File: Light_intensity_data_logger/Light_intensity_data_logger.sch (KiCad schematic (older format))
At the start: 23 parts, among them J1 Wire_to_Vbat, Q1 NTJD4001NT1G, Q2 NTJD4001NT1G, U1 BME280, U2 TCS34725FN, U3 TSL25911FN, U4 Teensy3.6

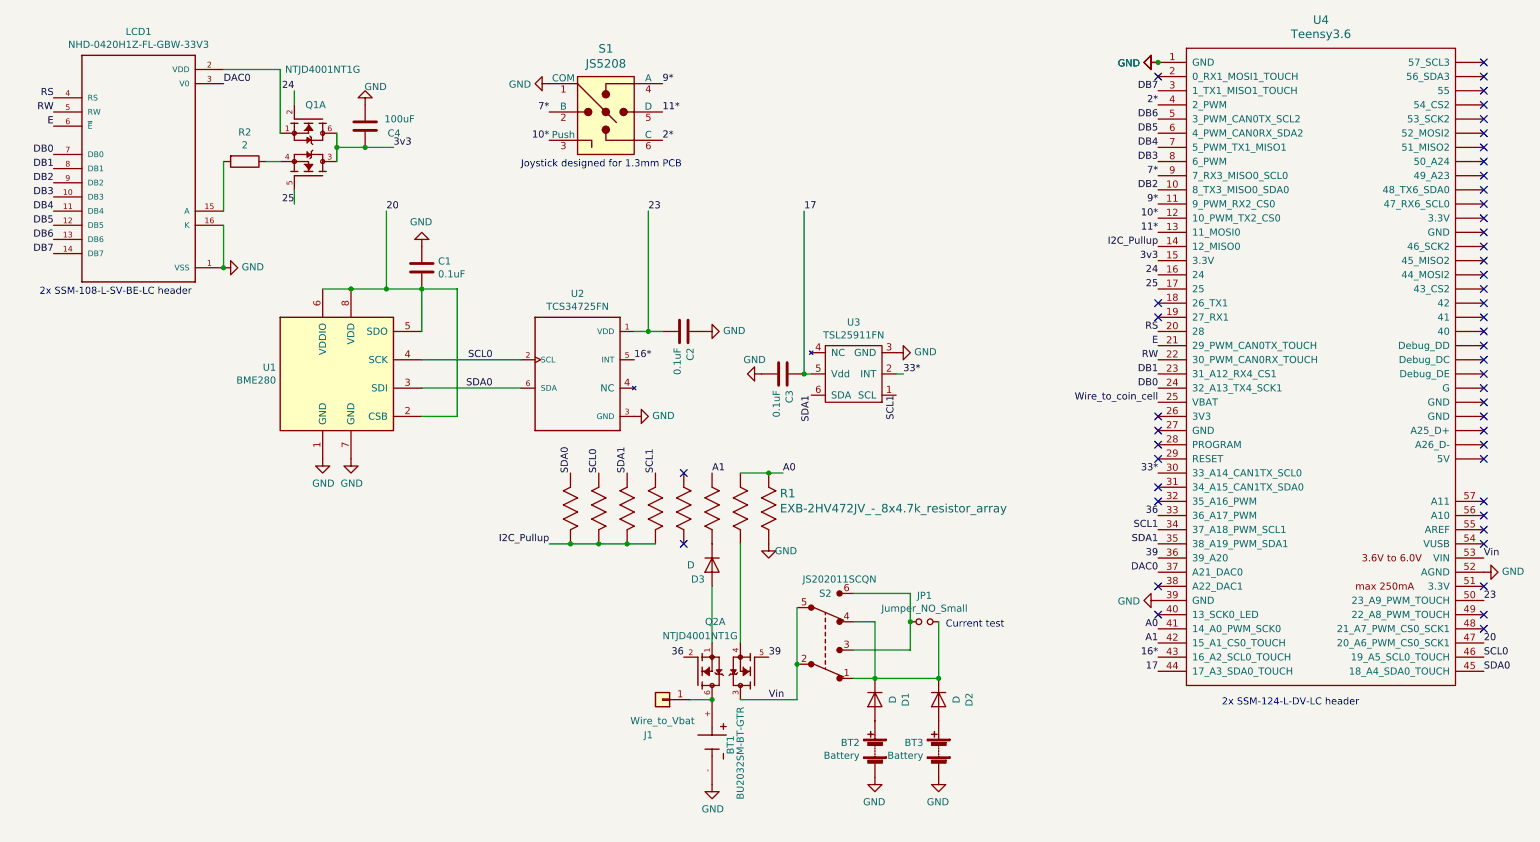
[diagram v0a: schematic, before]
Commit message: Rewire LED gate to PWM channel
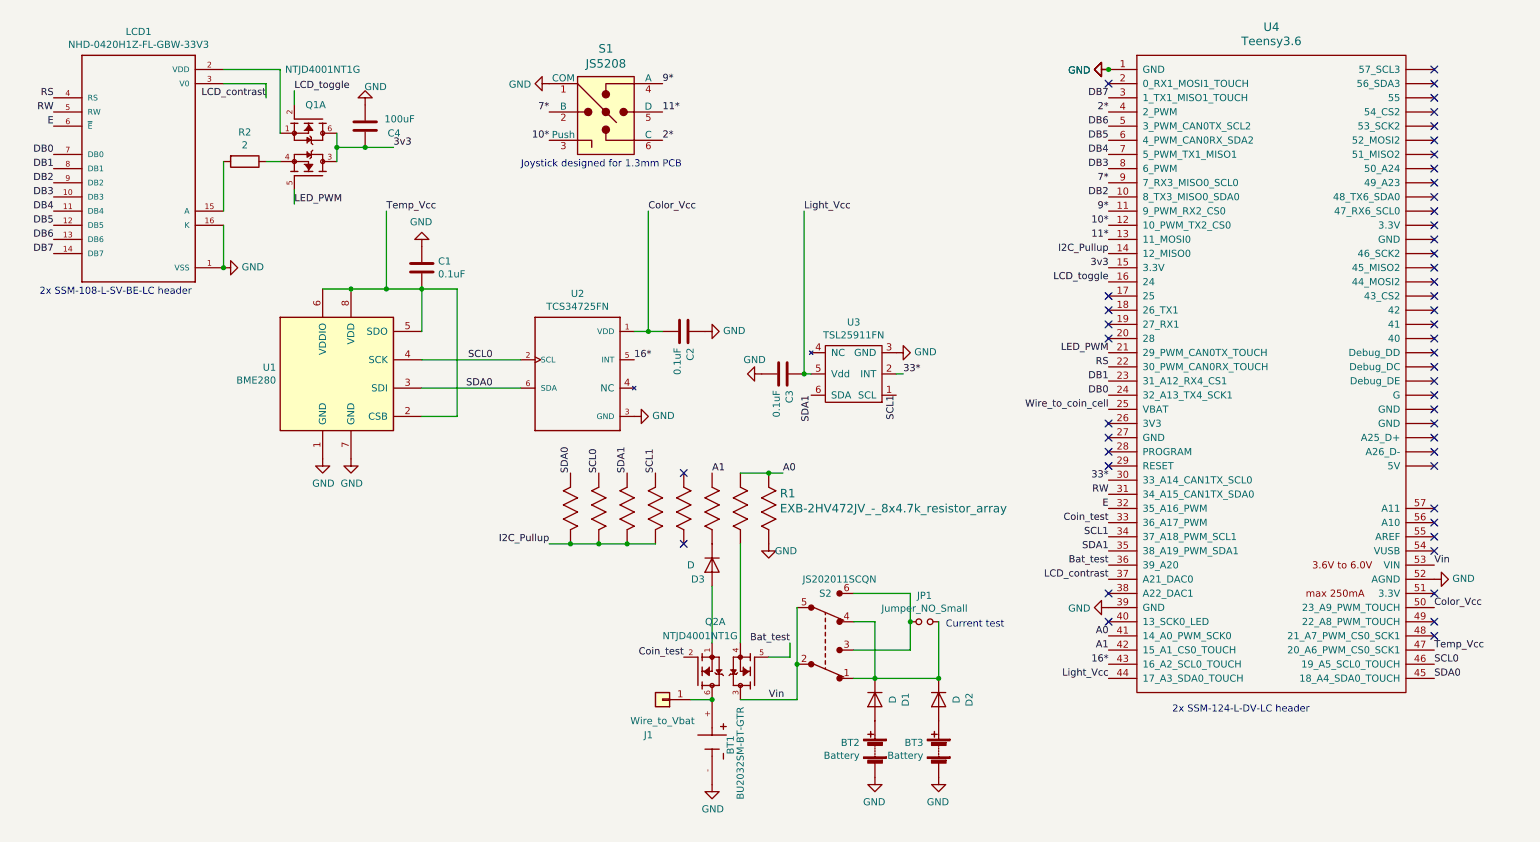
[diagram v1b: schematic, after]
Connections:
- net E: now also U4.32 (35_A16_PWM); no longer U4.21 (29_PWM_CAN0TX_TOUCH)
- net RS: now also U4.22 (30_PWM_CAN0RX_TOUCH); no longer U4.20 (28)
- net RW: now also U4.31 (34_A15_CAN1TX_SDA0); no longer U4.22 (30_PWM_CAN0RX_TOUCH)
- net 17 renamed Light_Vcc
- net 20 renamed Temp_Vcc
- net 23 renamed Color_Vcc
- net 24 renamed LCD_toggle
- net 25: no longer names the net of U4.17 (25)
- net 25: no longer Q1.5 (G2)
- net 36 renamed Coin_test
- net 39 renamed Bat_test
- net DAC0 renamed LCD_contrast
- new net LED_PWM: Q1.5 (G2), U4.21 (29_PWM_CAN0TX_TOUCH)
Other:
- moved on the sheet: U4

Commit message: Switch to 1uF caps for sensors per light sensor spec sheet
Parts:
- C1, C2, C3: value 0.1uF -> 1uF; Part# 311-1344-1-ND -> 445-1604-1-ND
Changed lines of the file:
@@
 P 3450 2300
 F 0 "C1" H 3565 2346 50  0000 L CNN
-F 1 "0.1uF" H 3565 2255 50  0000 L CNN
+F 1 "1uF" H 3565 2255 50  0000 L CNN
 F 2 "Capacitors_SMD:C_0603" H 3488 2150 50  0001 C CNN
-F 3 "https://media.digikey.com/pdf/Data%20Sheets/Samsunghttps://www.yageo.com/upload/media/product/productsearch/datasheet/mlcc/UPY-GPHC_X7R_6.3V-to-50V_18.pdf" H 3450 2300 50  0001 C CNN
-F 4 "311-1344-1-ND" H 3450 2300 50  0001 C CNN "Part#"
+F 3 "https://product.tdk.com/info/en/catalog/datasheets/mlcc_commercial_general_en.pdf?ref_disty=digikey" H 3450 2300 50  0001 C CNN
+F 4 "445-1604-1-ND" H 3450 2300 50  0001 C CNN "Part#"
 	1    3450 2300
 	1    0    0    -1
@@
 7*
 NoConn ~ 5300 3750
-$Comp
-L device:C C2
-U 1 1 5E2CDF37
-P 5300 2750
-F 0 "C2" H 5415 2796 50  0000 L CNN
-F 1 "0.1uF" H 5415 2705 50  0000 L CNN
-F 2 "Capacitors_SMD:C_0603" H 5338 2600 50  0001 C CNN
-F 3 "https://media.digikey.com/pdf/Data%20Sheets/Samsunghttps://www.yageo.com/upload/media/product/productsearch/datasheet/mlcc/UPY-GPHC_X7R_6.3V-to-50V_18.pdf" H 5300 2750 50  0001 C CNN
-F 4 "311-1344-1-ND" H 5300 2750 50  0001 C CNN "Part#"
-	1    5300 2750
-	0    1    1    0
-$EndComp
-Connection ~ 6150 3050
-$Comp
-L device:C C3
-U 1 1 5E2CD370
-P 6000 3050
-F 0 "C3" H 6115 3096 50  0000 L CNN
-F 1 "0.1uF" H 6115 3005 50  0000 L CNN
-F 2 "Capacitors_SMD:C_0603" H 6038 2900 50  0001 C CNN
-F 3 "https://media.digikey.com/pdf/Data%20Sheets/Samsunghttps://www.yageo.com/upload/media/product/productsearch/datasheet/mlcc/UPY-GPHC_X7R_6.3V-to-50V_18.pdf" H 6000 3050 50  0001 C CNN
-F 4 "311-1344-1-ND" H 6000 3050 50  0001 C CNN "Part#"
-	1    6000 3050
-	0    1    1    0
-$EndComp
 Wire Wire Line
 	6150 1900 6150 3050
@@
 Text Label 8300 4900 2    50   ~ 0
 A0
+$Comp
+L device:C C2
+U 1 1 5E252D52
+P 5300 2750
+F 0 "C2" V 5150 2700 50  0000 L CNN
+F 1 "1uF" V 5450 2700 50  0000 L CNN
+F 2 "Capacitors_SMD:C_0603" H 5338 2600 50  0001 C CNN
+F 3 "https://product.tdk.com/info/en/catalog/datasheets/mlcc_commercial_general_en.pdf?ref_disty=digikey" H 5300 2750 50  0001 C CNN
+F 4 "445-1604-1-ND" H 5300 2750 50  0001 C CNN "Part#"
+	1    5300 2750
+	0    1    1    0
+$EndComp
+$Comp
+L device:C C3
+U 1 1 5E2531ED
+P 6000 3050
+F 0 "C3" V 5850 3000 50  0000 L CNN
+F 1 "1uF" V 6150 3000 50  0000 L CNN
+F 2 "Capacitors_SMD:C_0603" H 6038 2900 50  0001 C CNN
+F 3 "https://product.tdk.com/info/en/catalog/datasheets/mlcc_commercial_general_en.pdf?ref_disty=digikey" H 6000 3050 50  0001 C CNN
+F 4 "445-1604-1-ND" H 6000 3050 50  0001 C CNN "Part#"
+	1    6000 3050
+	0    1    1    0
+$EndComp
+Connection ~ 6150 3050
 $EndSCHEMATC

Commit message: Remove extra info from switch BOM
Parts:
- S1: Category Switches -> (none); DK_Datasheet_Link http://spec_sheets.e-switch.com/specs/P200020.pdf -> (none); DK_Detail_Page /product-detail/en/e-switch/JS5208/EG4561-ND/1739634 -> (none); Description SWITCH NAVIGATION 20MA 15V -> (none); Digi-Key_PN EG4561-ND -> (none); Family Navigation Switches, Joystick -> (none); MPN JS5208 -> (none); Manufacturer E-Switch -> (none); Part# (none) -> EG4561-ND; Status Active -> (none)
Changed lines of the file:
@@
 F 2 "digikey-footprints:Switch_Nav_12.4x12.4mm_SMD_JS5208" H 4950 1400 60  0001 L CNN
 F 3 "http://spec_sheets.e-switch.com/specs/P200020.pdf" H 4950 1500 60  0001 L CNN
-F 4 "EG4561-ND" H 4950 1600 60  0001 L CNN "Digi-Key_PN"
-F 5 "JS5208" H 4950 1700 60  0001 L CNN "MPN"
-F 6 "Switches" H 4950 1800 60  0001 L CNN "Category"
-F 7 "Navigation Switches, Joystick" H 4950 1900 60  0001 L CNN "Family"
-F 8 "http://spec_sheets.e-switch.com/specs/P200020.pdf" H 4950 2000 60  0001 L CNN "DK_Datasheet_Link"
-F 9 "/product-detail/en/e-switch/JS5208/EG4561-ND/1739634" H 4950 2100 60  0001 L CNN "DK_Detail_Page"
-F 10 "SWITCH NAVIGATION 20MA 15V" H 4950 2200 60  0001 L CNN "Description"
-F 11 "E-Switch" H 4950 2300 60  0001 L CNN "Manufacturer"
-F 12 "Active" H 4950 2400 60  0001 L CNN "Status"
+F 4 "EG4561-ND" H 4950 1600 60  0001 L CNN "Part#"
 	1    4750 1200
 	1    0    0    -1

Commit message: PCBWay compatible - max PCB dim <100mm
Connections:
- net Vin: now also JP1.1, S2.3, S2.6
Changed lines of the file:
@@
 $EndComp
 Connection ~ 6150 3050
+Wire Wire Line
+	6100 4700 6100 4400
+Wire Wire Line
+	6100 4400 6900 4400
+Wire Wire Line
+	6900 4400 6900 4600
+Connection ~ 6100 4700
+Connection ~ 6900 4600
 $EndSCHEMATC

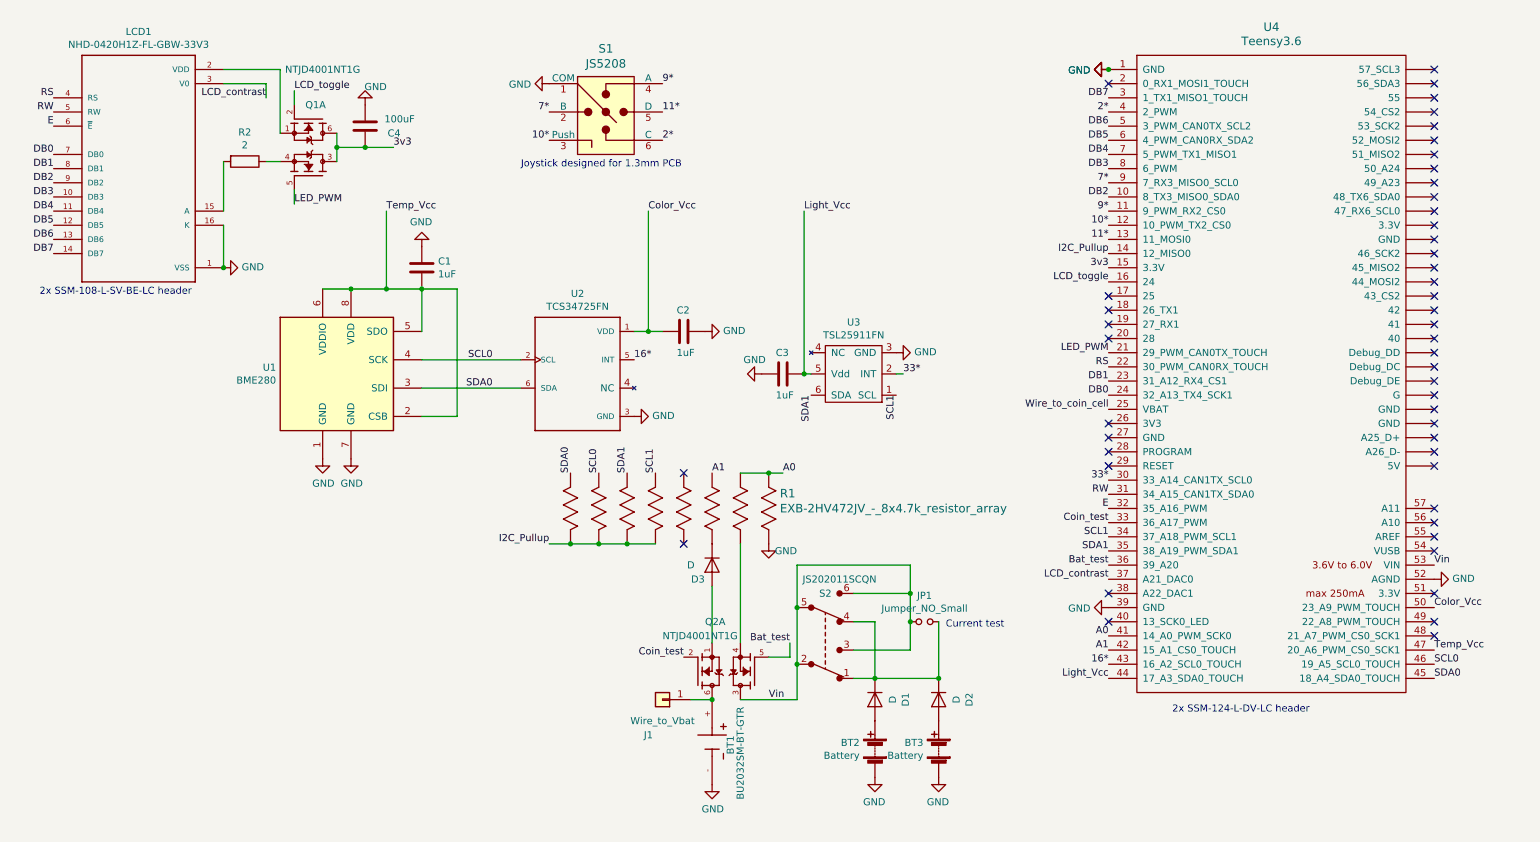
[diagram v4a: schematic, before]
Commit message: Fixed MOSFET issue - improved routing
Changed LCD to 4-pin only to free up pins
Routed data lines in clusters to leave open contiguous blocks of pins
Kept DAC0 line above PCB
Attached light interrupt to pin 21 - valid hibernate digital line
Used analog switch to pulse Vbat to DAC,
Put N-mos on GND side of LED.
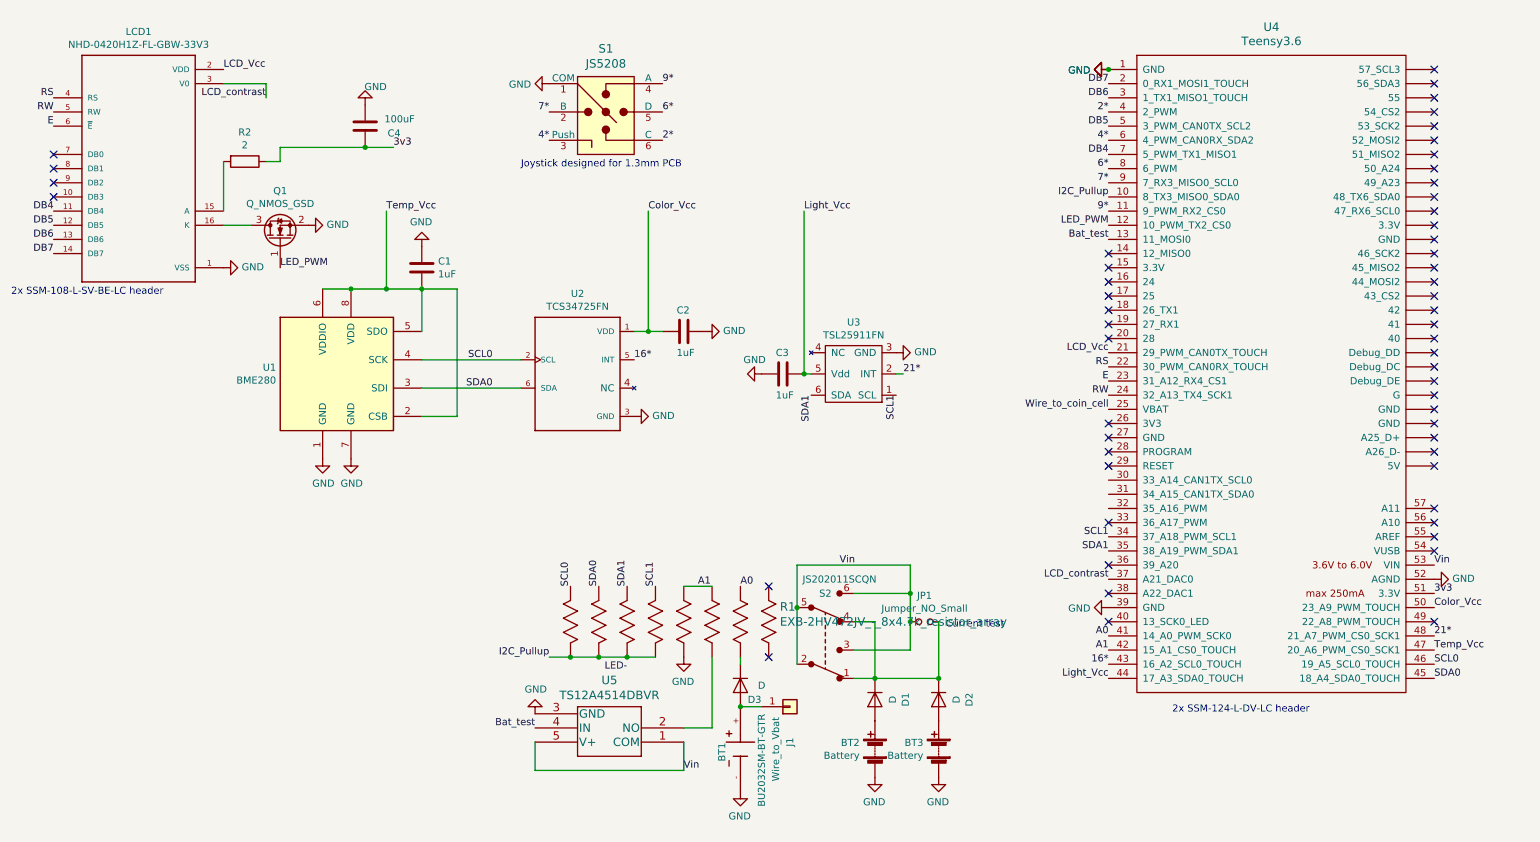
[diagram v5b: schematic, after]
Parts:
- removed Q1, Q2: NTJD4001NT1G, TO_SOT_Packages_SMD:SOT-363_SC-70-6, symbol Ben_custom:NTJD4001NT1G
- added Q1: Q_NMOS_GSD, TO_SOT_Packages_SMD:SOT-23, symbol device:Q_NMOS_GSD
- added U5: TS12A4514DBVR, TO_SOT_Packages_SMD:SOT-23-5, symbol Ben_custom:TS12A4514DBVR
- R1: footprint Ben_Custom:Resistor_array_1506_8x -> Ben_Custom:4816P-1-472LF; Part# Y1472CT-ND -> 4816P-1-472LFCT-ND
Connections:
- net 3v3: now also R2.1, U4.51 (3.3V); no longer U4.15 (3.3V)
- net A0: no longer R1.1
- net A1: now also R1.4
- net Bat_test: now also U4.13 (11_MOSI0), U5.4 (IN); no longer U4.36 (39_A20)
- net DB5: now also U4.5 (3_PWM_CAN0TX_SCL2); no longer U4.6 (4_PWM_CAN0RX_SDA2)
- net DB6: now also U4.3 (1_TX1_MISO1_TOUCH); no longer U4.5 (3_PWM_CAN0TX_SCL2)
- net DB7: now also U4.2 (0_RX1_MOSI1_TOUCH); no longer U4.3 (1_TX1_MISO1_TOUCH)
- net E: now also U4.23 (31_A12_RX4_CS1); no longer U4.32 (35_A16_PWM)
- net GND: now also R1.13, Q1.2 (S), U5.3 (GND); no longer LCD1.16 (K), R1.16
- net I2C_Pullup: now also U4.10 (8_TX3_MISO0_SDA0); no longer U4.14 (12_MISO0)
- net LED_PWM: now also U4.12 (10_PWM_TX2_CS0), Q1.1 (G); no longer U4.21 (29_PWM_CAN0TX_TOUCH)
- net RW: now also U4.24 (32_A13_TX4_SCK1); no longer U4.31 (34_A15_CAN1TX_SDA0)
- net SCL0: now also R1.8; no longer R1.7
- net SDA0: now also R1.7; no longer R1.8
- net Vin: now also U5.1 (COM), U5.5 (V+)
- net at BT1.+, J1.1 (Pin_1): now also D3.2 (A)
- net LCD_Vcc: now reaches LCD1.2 (VDD)
- net LCD_Vcc: now also U4.21 (29_PWM_CAN0TX_TOUCH)
- net at R1.15: now also D3.1 (K)
- net at R1.14: now also U5.2 (NO); no longer D3.1 (K)
- net 21*: now reaches U4.48 (21_A7_PWM_CS0_SCK1)
- net 21*: now also U3.2 (INT)
- net 10* renamed 4*
- net 4*: now also U4.6 (4_PWM_CAN0RX_SDA2); no longer U4.12 (10_PWM_TX2_CS0)
- net 11* renamed 6*
- net 6*: now also U4.8 (6_PWM); no longer U4.13 (11_MOSI0)
- net 33*: no longer names the net of U4.30 (33_A14_CAN1TX_SCL0)
- net 33*: no longer U3.2 (INT)
- net Coin_test: no longer names the net of U4.33 (36_A17_PWM)
- net DB0: no longer names the net of LCD1.7 (DB0)
- net DB0: no longer U4.24 (32_A13_TX4_SCK1)
- net DB1: no longer names the net of LCD1.8 (DB1)
- net DB1: no longer U4.23 (31_A12_RX4_CS1)
- net DB2: no longer names the net of LCD1.9 (DB2)
- net DB2: no longer U4.10 (8_TX3_MISO0_SDA0)
- net DB3: no longer names the net of LCD1.10 (DB3)
- net DB3: no longer U4.8 (6_PWM)
- net LCD_toggle: no longer names the net of U4.16 (24)
- new net: LCD1.16 (K), Q1.3 (D)
- no-connect marks 49 -> 55
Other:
- moved on the sheet: BT1, D3, J1, R1

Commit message: This is draft of PCB submitted to PCBWay, logging works!!!
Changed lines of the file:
@@
 	0    -1   -1   0
 $EndComp
-Text Label 4900 5150 2    50   ~ 0
-LED-
 Text Label 10600 4600 0    50   ~ 0
 3v3

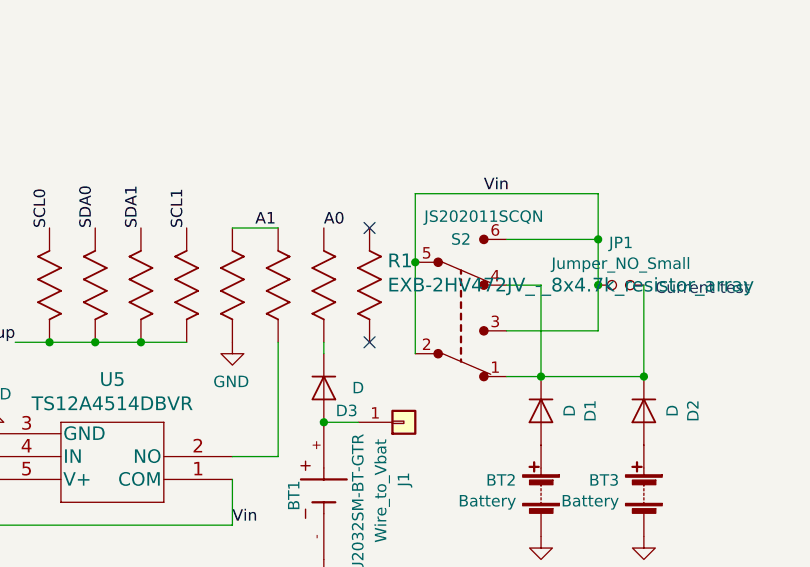
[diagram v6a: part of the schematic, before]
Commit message: Add pulldown resistor to LCD LED PWM pin
Add pull down resistor so that the LCD LED with default to off if the pin is in a high impedance state.
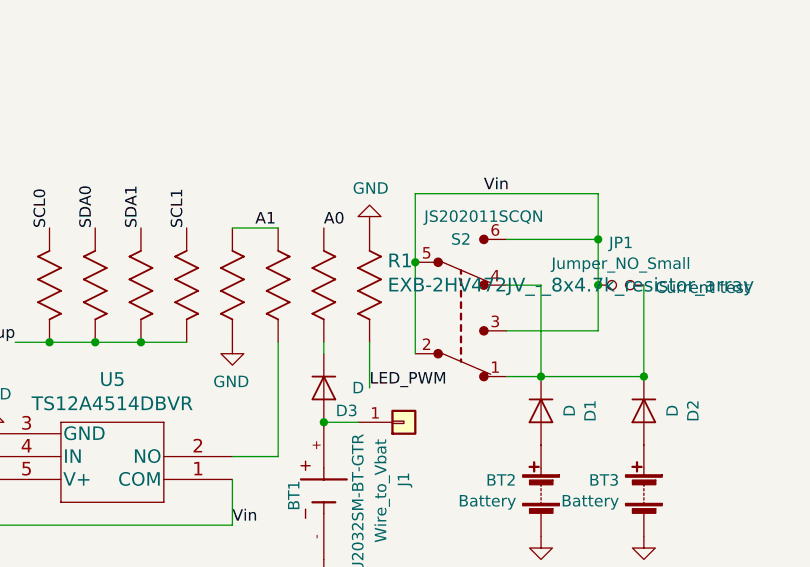
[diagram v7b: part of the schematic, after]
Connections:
- net GND: now also R1.1
- net LED_PWM: now also R1.16
- no-connect marks 55 -> 53
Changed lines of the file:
@@
 Wire Wire Line
 	5700 5050 5700 5100
-NoConn ~ 5900 4550
-NoConn ~ 5900 5050
 Wire Wire Line
 	5500 4550 5300 4550
@@
 Wire Wire Line
 	5500 5550 5500 5050
+Text Label 5900 5250 0    50   ~ 0
+LED_PWM
+Wire Wire Line
+	5900 5250 5900 5050
+$Comp
+L power:GND #PWR?
+U 1 1 5E575191
+P 5900 4550
+F 0 "#PWR?" H 5900 4300 50  0001 C CNN
+F 1 "GND" H 5905 4377 50  0000 C CNN
+F 2 "" H 5900 4550 50  0001 C CNN
+F 3 "" H 5900 4550 50  0001 C CNN
+	1    5900 4550
+	1    0    0    1
+$EndComp
 $EndSCHEMATC
